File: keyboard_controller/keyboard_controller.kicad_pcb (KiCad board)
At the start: 2 copper layers, 43.2 x 34.3 mm, 2 parts, among them J4 Conn_01x30, U1 Teensy2.0

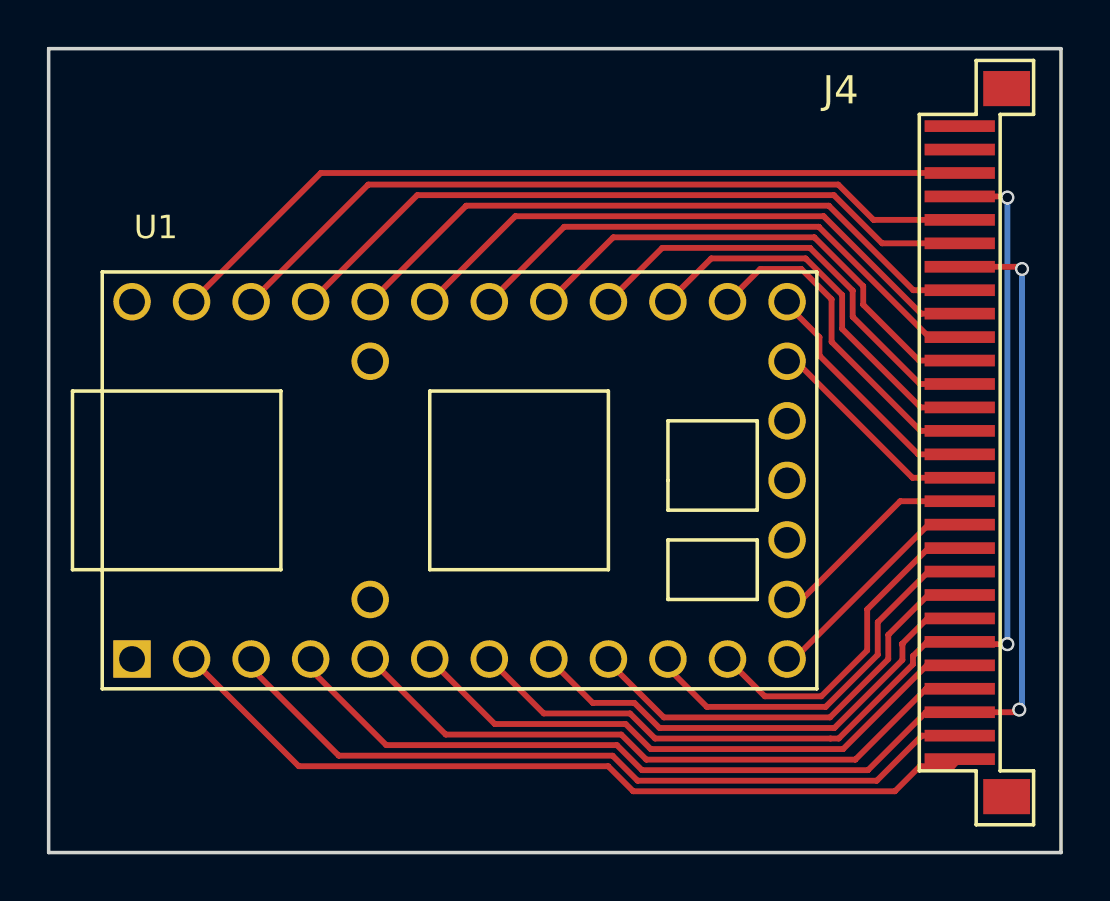
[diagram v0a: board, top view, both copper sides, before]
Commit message: Small fixups, smaller outline, gerber generation settings changed
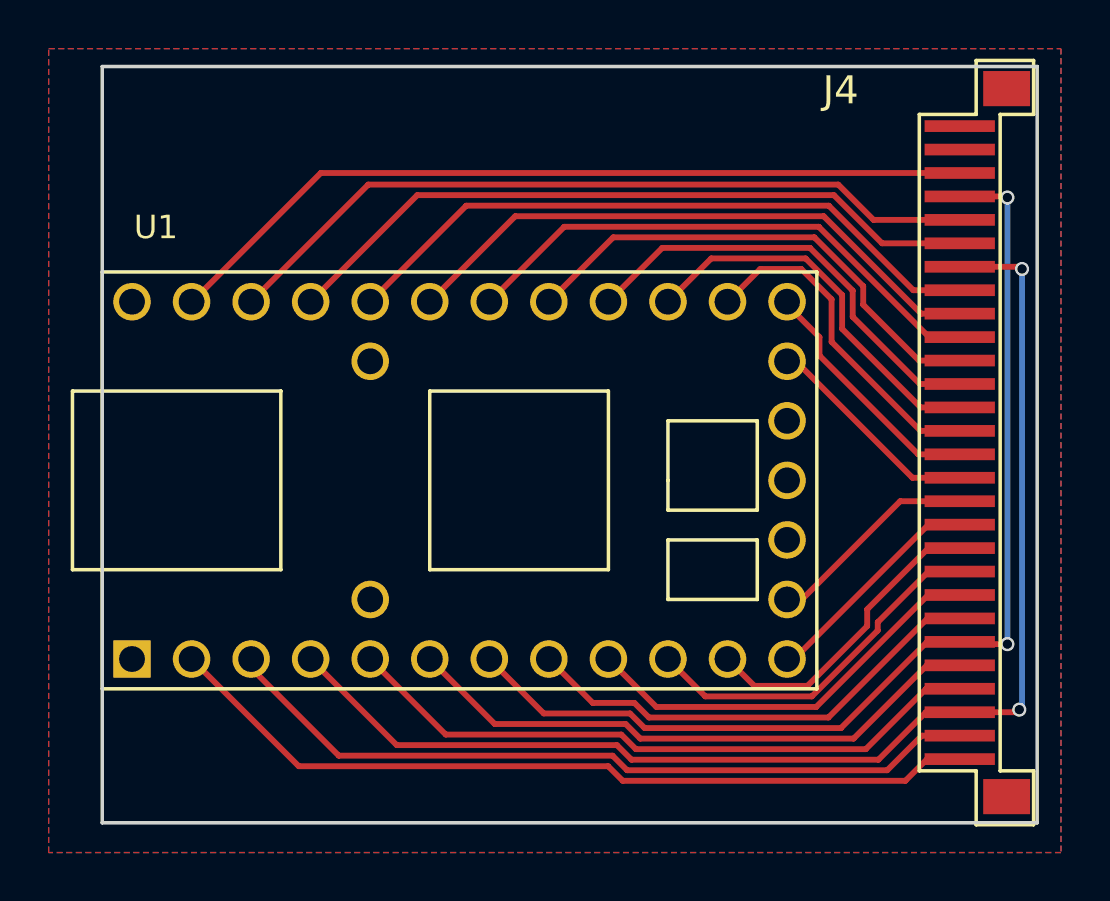
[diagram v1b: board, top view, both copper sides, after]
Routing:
- net COL3: track 16.7 -> 15.5 mm
- net ROW4: track 20.2 -> 19.1 mm
- net ROW5: track 14.2 -> 13.2 mm
- net COL2: track 21.1 -> 20.3 mm
- net ROW1: track 55.1 -> 54.4 mm
- net ROW3: track 46.6 -> 46.0 mm
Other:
- board size 43.2 x 34.3 mm -> 39.9 x 32.3 mm
